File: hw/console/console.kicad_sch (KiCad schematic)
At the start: 59 parts, among them J1 Batt, SW1 Движок, SW2 RESET, U1 F133-A, U2 SY8089AAAC, U3 SY8089AAAC, U4 SY8089AAAC, U5 TP4056, Y1 24 МГц, Y2 32.768 кГц

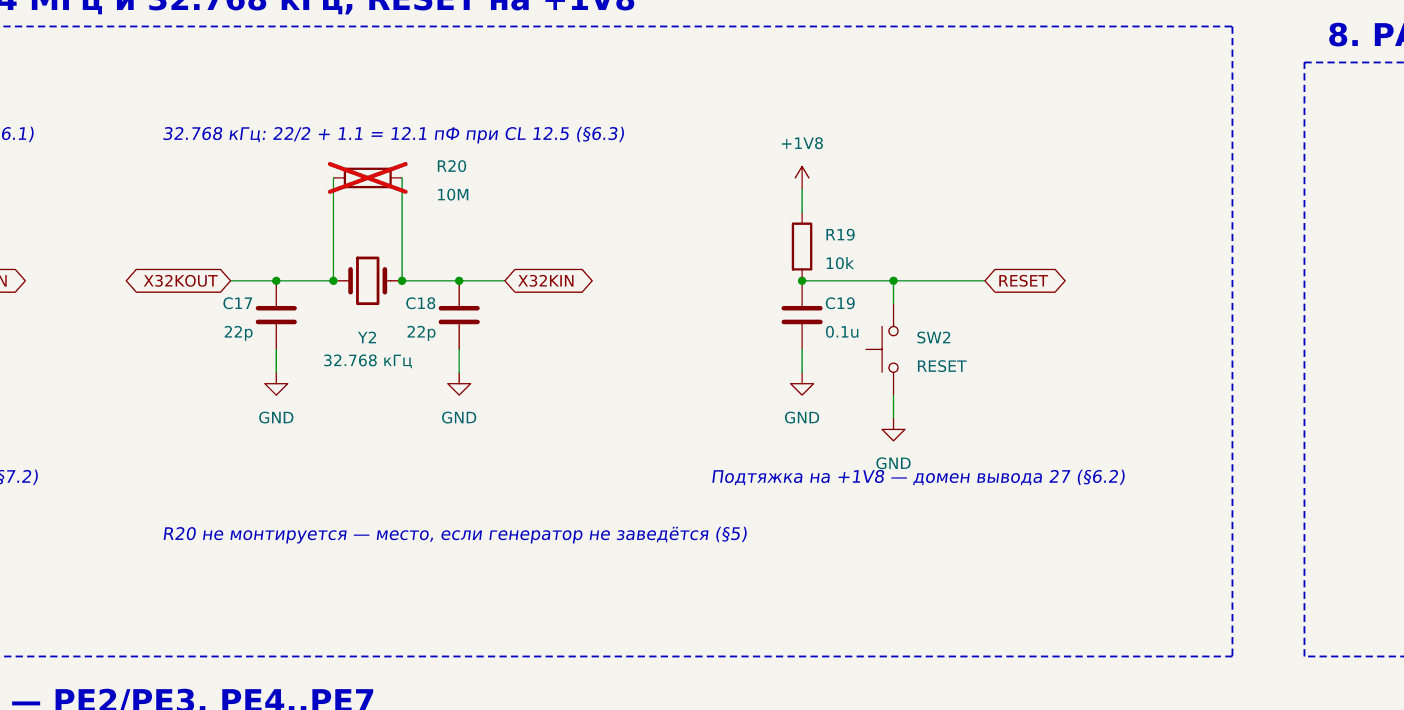
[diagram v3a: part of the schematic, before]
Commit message: hw: прогон блока 7 — неверно прочитана схема MangoPi, резистор смещения нужен
Я записал в §3, что у MangoPi нет резистора параллельно кварцу 32.768 кГц, и
на этом построил решение: деталь на схеме есть, но не монтируется (DNP).

При перепроверке на кропе 400 dpi видно четыре точки соединения: R40 680K 1%
сидит на той же паре узлов, что и XT1, то есть **параллельно кварцу**. Резистор
ставят обе платы, расходятся они только номиналом — 680K у MangoPi, 10M у
Xassette. В первый раз R40 был принят за делитель соседнего buck'а: там
действительно стоит 680K 1%, и по номиналу они неотличимы.

Исправлено: R20 = 680k и монтируется. Даташит про этот резистор молчит совсем,
поэтому в §7.5 записано, чем рискуем: чем меньше номинал, тем сильнее раскачка,
а часовые кварцы чувствительны к перекачке. Разница между платами
пятнадцатикратная и объяснить её нечем — берём MangoPi как серийный и на том же
чипе.

На кварце 24 МГц резистора нет ни у одной платы — проверено на том же кропе.

Co-Authored-By: Claude Opus 5 <noreply@anthropic.com>
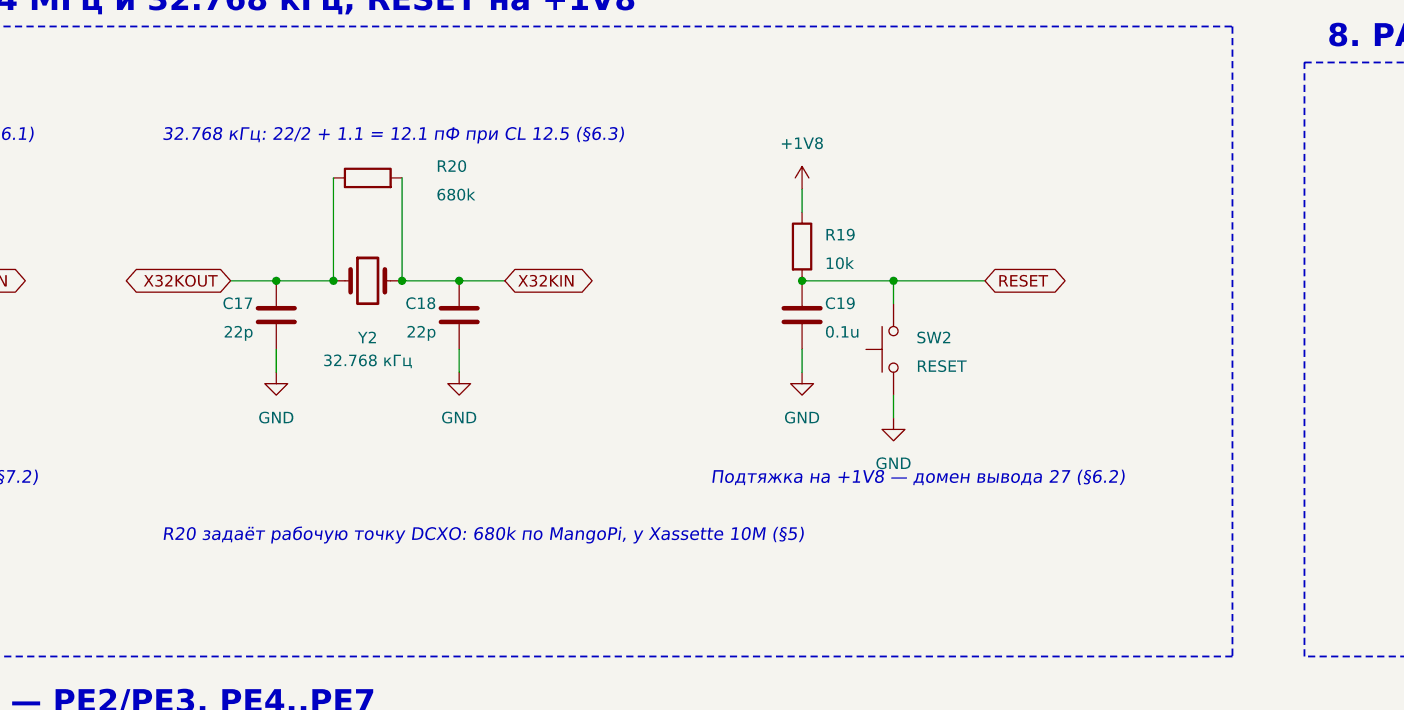
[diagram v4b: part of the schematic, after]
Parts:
- R20: value 10M -> 680k; now fitted
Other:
- note added: "R20 задаёт рабочую точку DCXO: 680k по MangoPi, у Xassette 10M (§5)"
- note removed: "R20 не монтируется — место, если генератор не заведётся (§5)"
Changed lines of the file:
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@@
 		(in_bom yes)
 		(on_board yes)
-		(dnp yes)
+		(dnp no)
 		(property "Reference" "R20"
 			(at 129.54 289.56 270)
@@
 			)
 		)
-		(property "Value" "10M"
+		(property "Value" "680k"
 			(at 129.54 292.735 270)
 			(effects
@@
 		(effects (font (size 1.4 1.4) (italic yes)) (justify left bottom))
 	)
-	(text "R20 не монтируется — место, если генератор не заведётся (§5)"
+	(text "R20 задаёт рабочую точку DCXO: 680k по MangoPi, у Xassette 10M (§5)"
 		(exclude_from_sim yes)
 		(at 99.06 331.47 0)

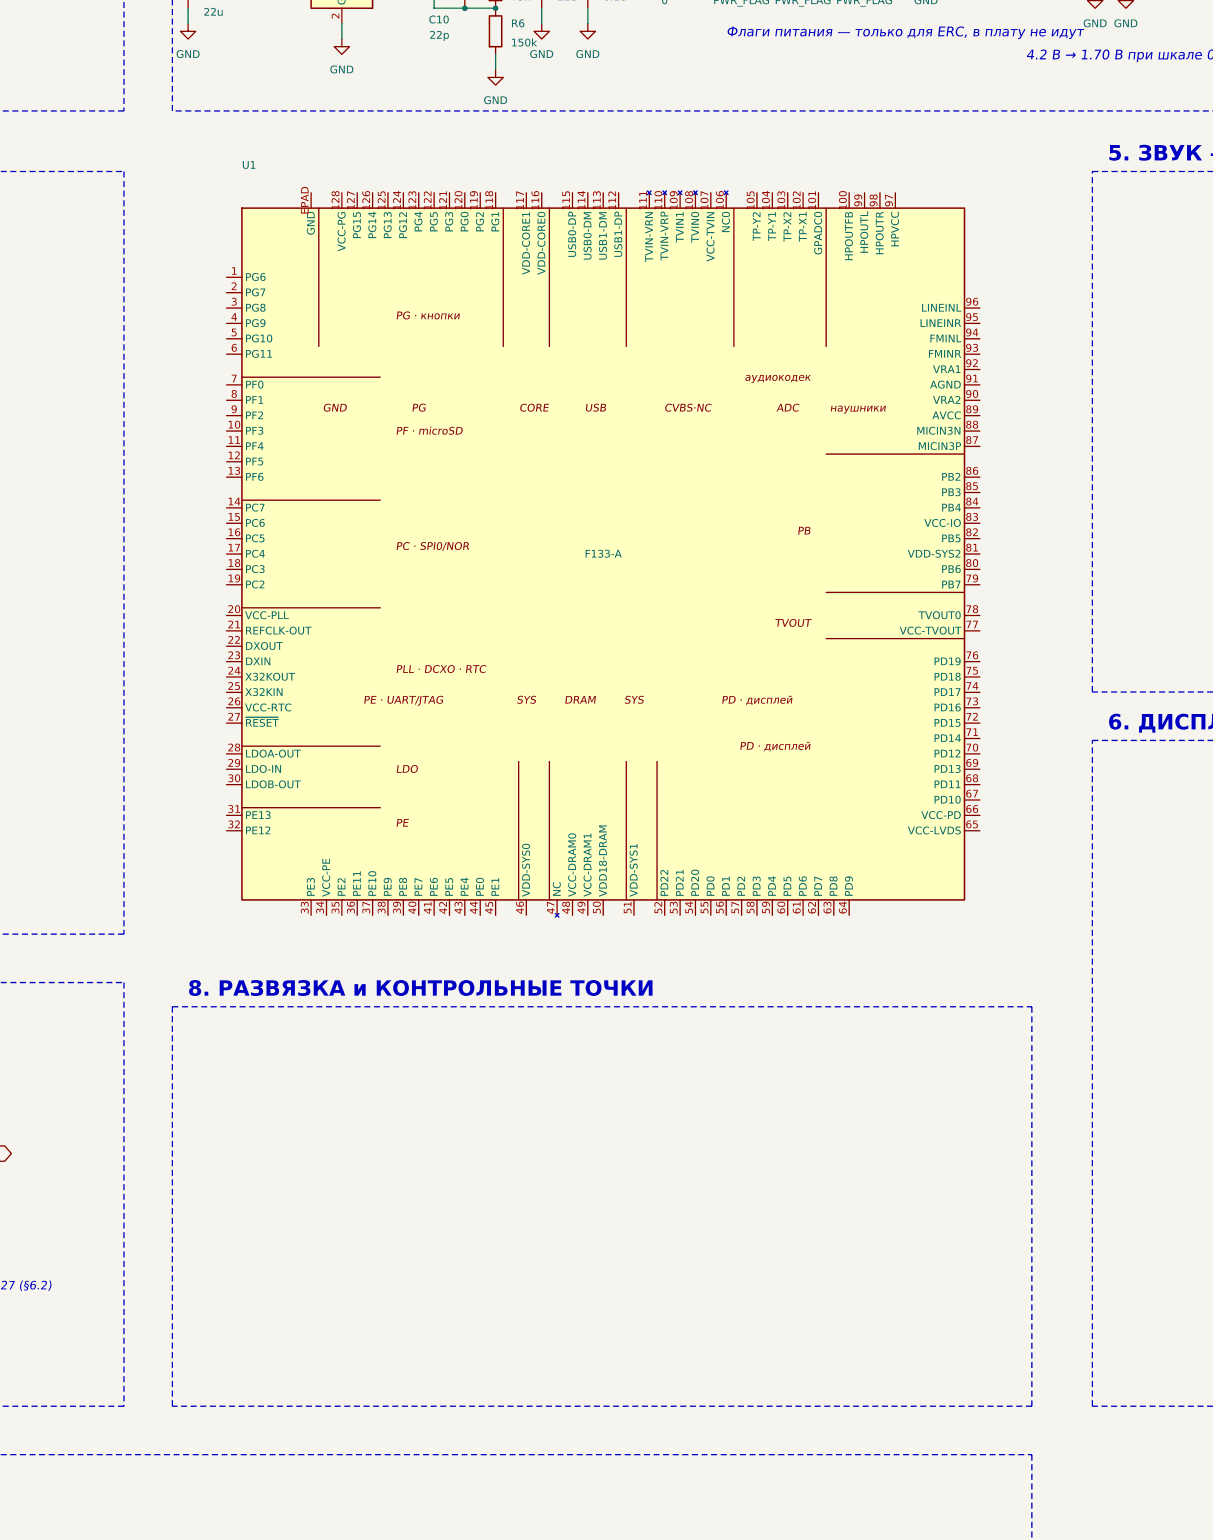
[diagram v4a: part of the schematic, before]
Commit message: hw: блок 8 «Развязка и контрольные точки» нарисован
Развязка F133: по 0.1 мкФ на каждый из 18 выводов питания, объёмный 10 мкФ
на рельсу у корпуса, конденсаторы внутренних LDO, аналоговая земля кодека
через 0 Ω, контрольные точки на REFCLK и земле. 33 детали. ERC упал со 160
нарушений до 104, все оставшиеся — на невыведенных выводах F133, кроме VBUS
из будущего блока 3.

Две правки распиновки, обе из-за дочитанной сноски к Table 4-2:

- вывод 107 VCC-TVIN у F133-A **NC** — сноска перечисляет 107..111 поимённо,
  питание блока CVBS IN в списке наравне с сигналами. Обе референсные платы
  его подключают, потому что рисовались и под F133-B. Убран из +1V8;
- вывод 47 переведён в passive: даташит зовёт его NC, но и MangoPi, и
  Xassette вешают туда 240 Ω с именем DZQ. Ставим — если NC верно, резистор
  ни на что не влияет, если нет, без него не пройдёт калибровка DDR2.

Новый tools/mangopi_net.py: читает PDF-схему MangoPi как схему, а не как
картинку. pdftocairo -svg отдаёт точные концы отрезков, цепи собираются
union-find'ом, касание считается соединением только при наличии точки.
Заведён после двух подряд неверных чтений кропов глазами.

gen_f133_sym.py теперь синхронизирует и вшитую в схему копию символа:
KiCad библиотеку при открытии не перечитывает, и правка распиновки иначе
разъезжается молча.

Co-Authored-By: Claude Opus 5 <noreply@anthropic.com>
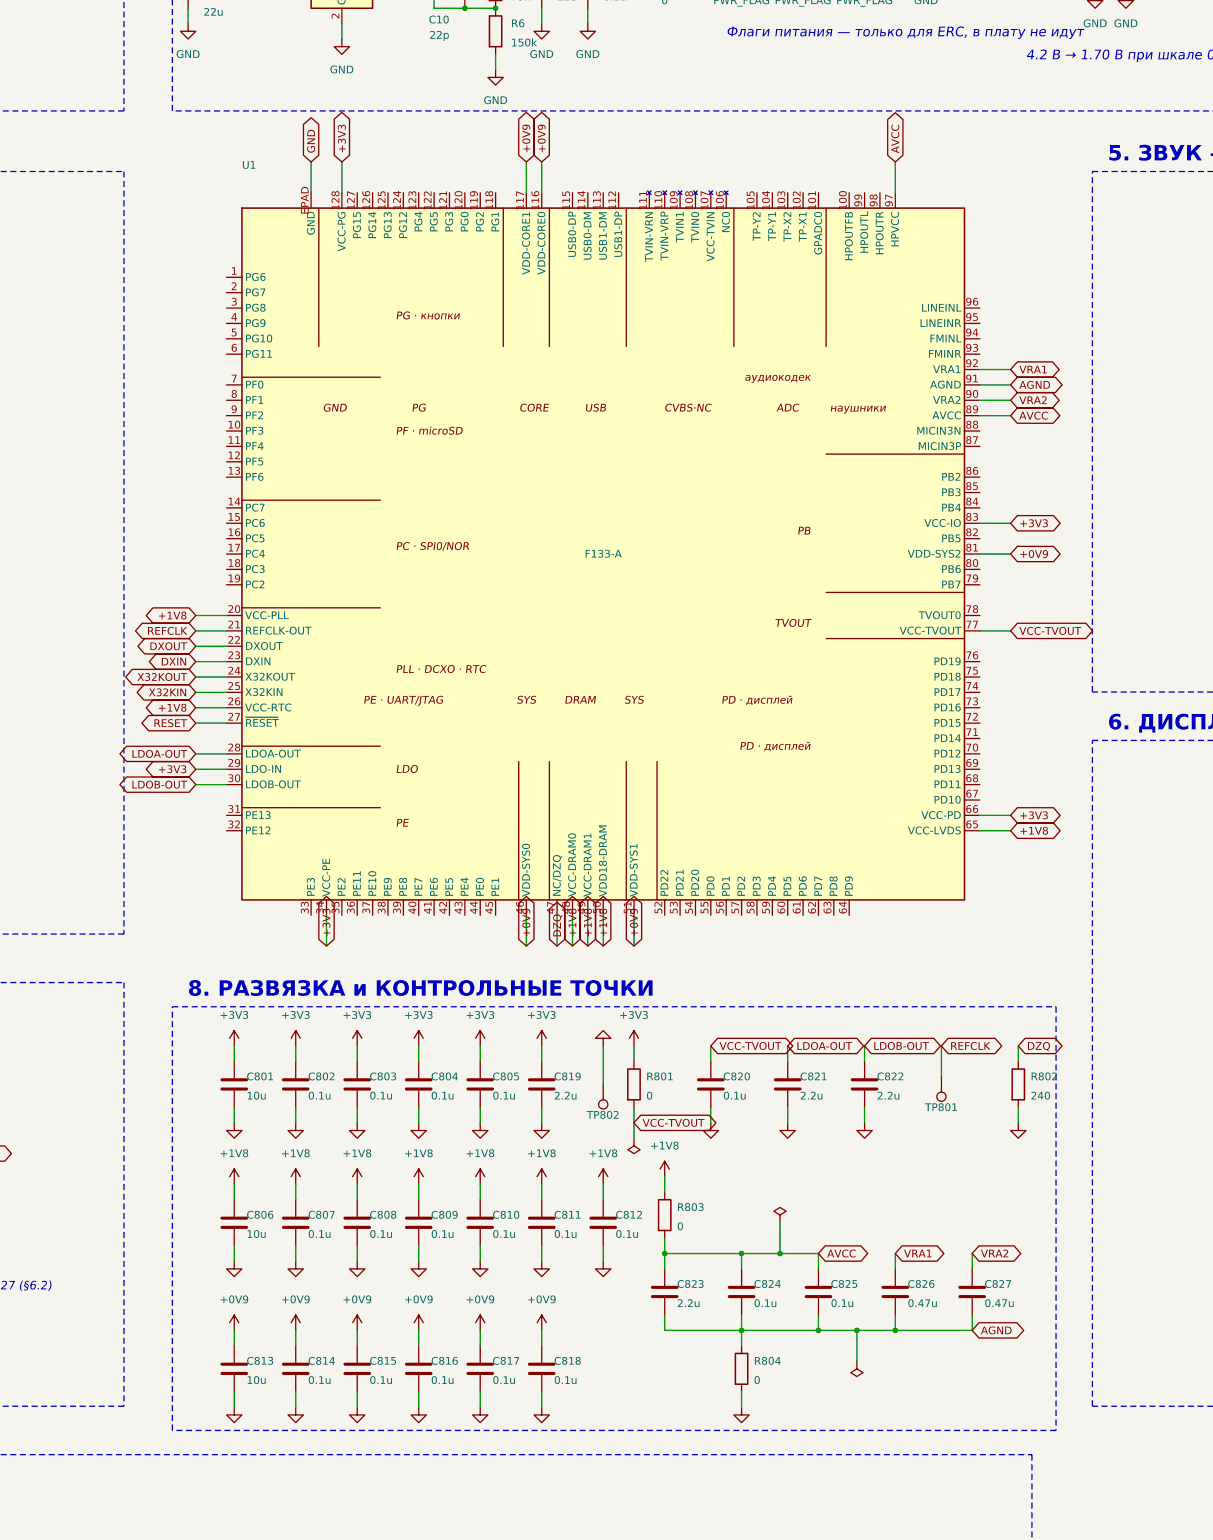
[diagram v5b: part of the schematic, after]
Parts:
- added C801, C806, C813: 10u, Capacitor_SMD:C_0805_2012Metric_Pad1.18x1.45mm_HandSolder, symbol Device:C
- added C802, C803, C804, C805, C807, C808, C809, C810, C811, C812, C814, C815, C816, C817, C818, C820, C824, C825: 0.1u, Capacitor_SMD:C_0805_2012Metric_Pad1.18x1.45mm_HandSolder, symbol Device:C
- added C819, C821, C822, C823: 2.2u, Capacitor_SMD:C_0805_2012Metric_Pad1.18x1.45mm_HandSolder, symbol Device:C
- added C826, C827: 0.47u, Capacitor_SMD:C_0805_2012Metric_Pad1.18x1.45mm_HandSolder, symbol Device:C
- added R801, R803, R804: 0, Resistor_SMD:R_0805_2012Metric_Pad1.20x1.40mm_HandSolder, symbol Device:R
- added R802: 240, Resistor_SMD:R_0805_2012Metric_Pad1.20x1.40mm_HandSolder, symbol Device:R
- added TP801: REFCLK, TestPoint:TestPoint_Pad_D1.5mm, symbol Connector:TestPoint
- added TP802: GND, TestPoint:TestPoint_Pad_D1.5mm, symbol Connector:TestPoint
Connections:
- net +0V9: now also U1.116 (VDD-CORE0), U1.117 (VDD-CORE1), U1.46 (VDD-SYS0), U1.51 (VDD-SYS1), U1.81 (VDD-SYS2), C813.1, C814.1, C815.1, C816.1, C817.1, C818.1
- net +1V8: now also U1.20 (VCC-PLL), U1.26 (VCC-RTC), U1.48 (VCC-DRAM0), U1.49 (VCC-DRAM1), U1.50 (VDD18-DRAM), U1.65 (VCC-LVDS), C806.1, C807.1, C808.1, C809.1, C810.1, C811.1, C812.1, R803.1
- net +3V3: now also U1.128 (VCC-PG), U1.29 (LDO-IN), U1.34 (VCC-PE), U1.66 (VCC-PD), U1.83 (VCC-IO), C801.1, C802.1, C803.1, C804.1, C805.1, C819.1, R801.1
- net DXIN: now also U1.23 (DXIN)
- net DXOUT: now also U1.22 (DXOUT)
- net GND: now also U1.EPAD (GND), C801.2, C802.2, C803.2, C804.2, C805.2, C806.2, C807.2, C808.2, C809.2, C810.2, C811.2, C812.2, C813.2, C814.2, C815.2, C816.2, C817.2, C818.2, C819.2, C820.2, C821.2, C822.2, R802.2, R804.2, TP802.1
- net RESET: now also U1.27 (~{RESET})
- net X32KIN: now also U1.25 (X32KIN)
- net X32KOUT: now also U1.24 (X32KOUT)
- net REFCLK: now reaches U1.21 (REFCLK-OUT)
- net REFCLK: now also TP801.1
- net LDOA-OUT: now reaches U1.28 (LDOA-OUT)
- net LDOA-OUT: now also C821.1
- net LDOB-OUT: now reaches U1.30 (LDOB-OUT)
- net LDOB-OUT: now also C822.1
- net DZQ: now reaches U1.47 (NC/DZQ)
- net DZQ: now also R802.1
- net VCC-TVOUT: now reaches U1.77 (VCC-TVOUT)
- net VCC-TVOUT: now also C820.1, R801.2
- net AVCC: now reaches U1.89 (AVCC)
- net AVCC: now also U1.97 (HPVCC), C823.1, C824.1, C825.1, R803.2
- net VRA2: now reaches U1.90 (VRA2)
- net VRA2: now also C827.1
- net AGND: now reaches U1.91 (AGND)
- net AGND: now also C823.2, C824.2, C825.2, C826.2, C827.2, R804.1
- net VRA1: now reaches U1.92 (VRA1)
- net VRA1: now also C826.1
